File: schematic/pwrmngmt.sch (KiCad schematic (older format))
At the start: 16 parts, among them U6 MC34063AD, U7 TP4054

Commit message: updated resistor dividers for more friendly values
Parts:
- R13: value 3.6k -> 33k
- R14: value 2.2k -> 20k
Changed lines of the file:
@@
 AR Path="/61F4C378/6216BBEE" Ref="R14"  Part="1"
 F 0 "R14" H 7370 4646 50  0000 L CNN
-F 1 "2.2k" H 7370 4555 50  0000 L CNN
+F 1 "20k" H 7370 4555 50  0000 L CNN
 F 2 "Resistor_SMD:R_0805_2012Metric_Pad1.20x1.40mm_HandSolder" V 7230 4600 50  0001 C CNN
 F 3 "~" H 7300 4600 50  0001 C CNN
@@
 AR Path="/61F4C378/6216BC16" Ref="R13"  Part="1"
 F 0 "R13" H 7450 4250 50  0000 C CNN
-F 1 "3.6k" H 7450 4150 50  0000 C CNN
+F 1 "33k" H 7450 4150 50  0000 C CNN
 F 2 "Resistor_SMD:R_0805_2012Metric_Pad1.20x1.40mm_HandSolder" V 7230 4200 50  0001 C CNN
 F 3 "~" H 7300 4200 50  0001 C CNN

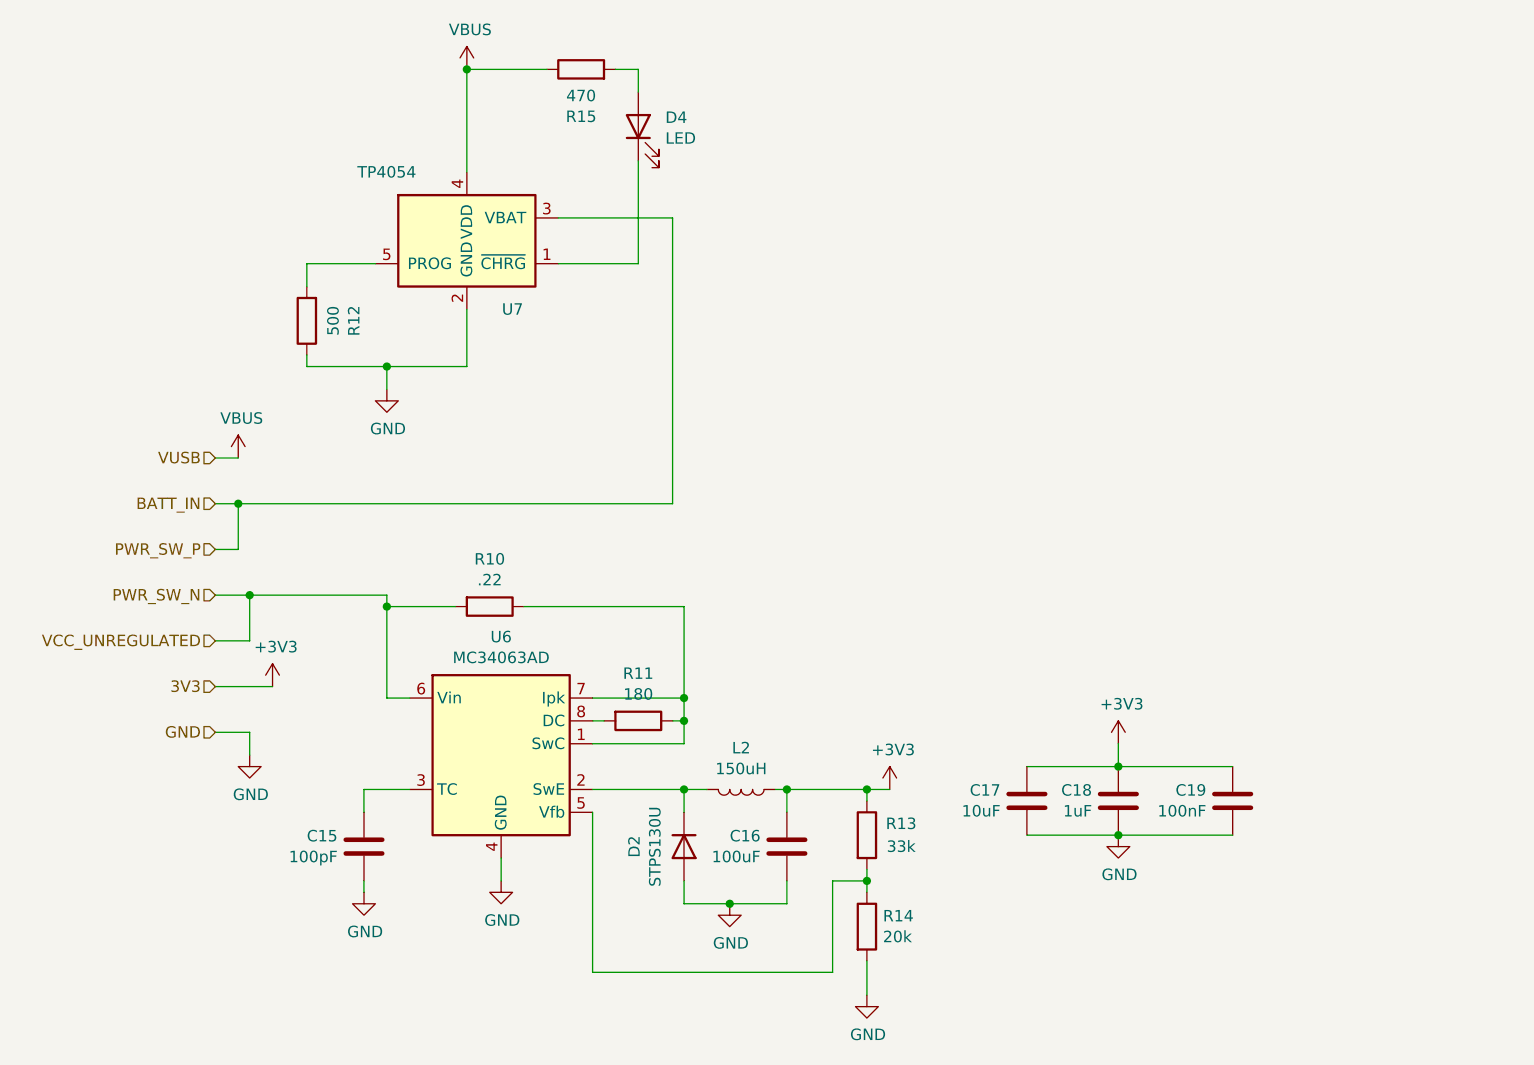
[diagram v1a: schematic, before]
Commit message: replacing buck converter with higher efficiency one
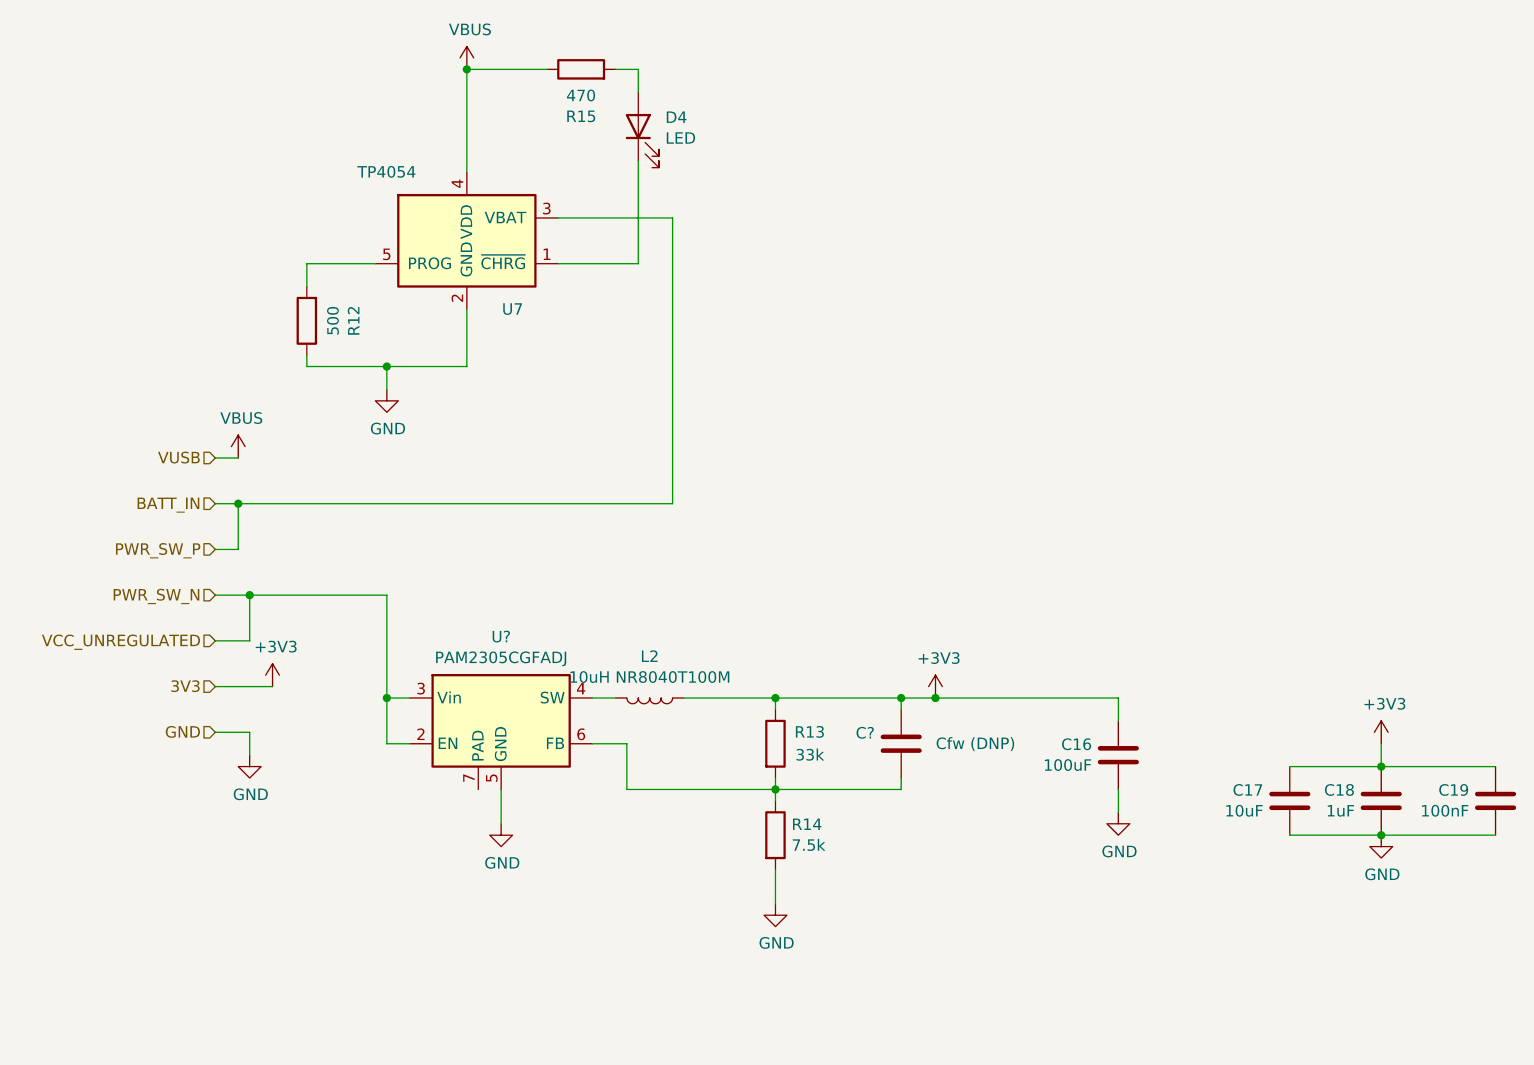
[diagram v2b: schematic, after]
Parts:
- removed C15: 100pF, Capacitor_SMD:C_0805_2012Metric_Pad1.18x1.45mm_HandSolder, symbol Device:C
- removed D2: STPS130U, Diode_SMD:D_SMB, symbol Device:D
- removed R10: .22, Resistor_SMD:R_0805_2012Metric_Pad1.20x1.40mm_HandSolder, symbol Device:R
- removed R11: 180, Resistor_SMD:R_0805_2012Metric_Pad1.20x1.40mm_HandSolder, symbol Device:R
- removed U6: MC34063AD, Package_SO:SOIC-8_3.9x4.9mm_P1.27mm, symbol Regulator_Switching:MC34063AD
- added C?: Cfw (DNP), Capacitor_SMD:C_0805_2012Metric_Pad1.18x1.45mm_HandSolder, symbol Device:C
- added U?: PAM2305CGFADJ, Package_DFN_QFN:DFN-6-1EP_2x2mm_P0.65mm_EP1x1.6mm, symbol Regulator_Switching:PAM2305CGFADJ
- L2: value 150uH -> 10uH NR8040T100M; footprint Inductor_SMD:L_6.3x6.3_H3 -> Inductor_SMD:L_Taiyo-Yuden_NR-80xx_HandSoldering
- R14: value 20k -> 7.5k
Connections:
- net +3V3: now also C?.1
- net GND: now also U?.5 (GND)
- net PWR_SW_N: now also U?.2 (EN), U?.3 (Vin)
- net at L2.2: now also U?.4 (SW)
- net at R13.2, R14.1: now also C?.2, U?.6 (FB)
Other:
- moved on the sheet: C16, C17, C18, C19, L2, R13, R14
